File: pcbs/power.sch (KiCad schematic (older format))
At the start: 0 parts

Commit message: LED driver part done.
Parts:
- added J?: Barrel_Jack, Connectors:BARREL_JACK, symbol Barrel_Jack
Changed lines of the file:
@@
 $Descr A4 11693 8268
 encoding utf-8
-Sheet 1 35
+Sheet 35 35
 Title ""
 Date ""
@@
 Comment4 ""
 $EndDescr
-$Sheet
-S 6400 1875 2125 2050
-U 5A0916C5
-F0 "LEDDriver" 60
-F1 "LEDDriver.sch" 60
-$EndSheet
-$Sheet
-S 2380 1810 2170 2300
-U 5A15F128
-F0 "Power" 60
-F1 "power.sch" 60
-$EndSheet
+$Comp
+L Barrel_Jack J?
+U 1 1 5A15F131
+P 1750 1350
+F 0 "J?" H 1750 1560 50  0000 C CNN
+F 1 "Barrel_Jack" H 1750 1175 50  0000 C CNN
+F 2 "Connectors:BARREL_JACK" H 1800 1310 50  0001 C CNN
+F 3 "" H 1800 1310 50  0001 C CNN
+	1    1750 1350
+	1    0    0    -1
+$EndComp
 $EndSCHEMATC

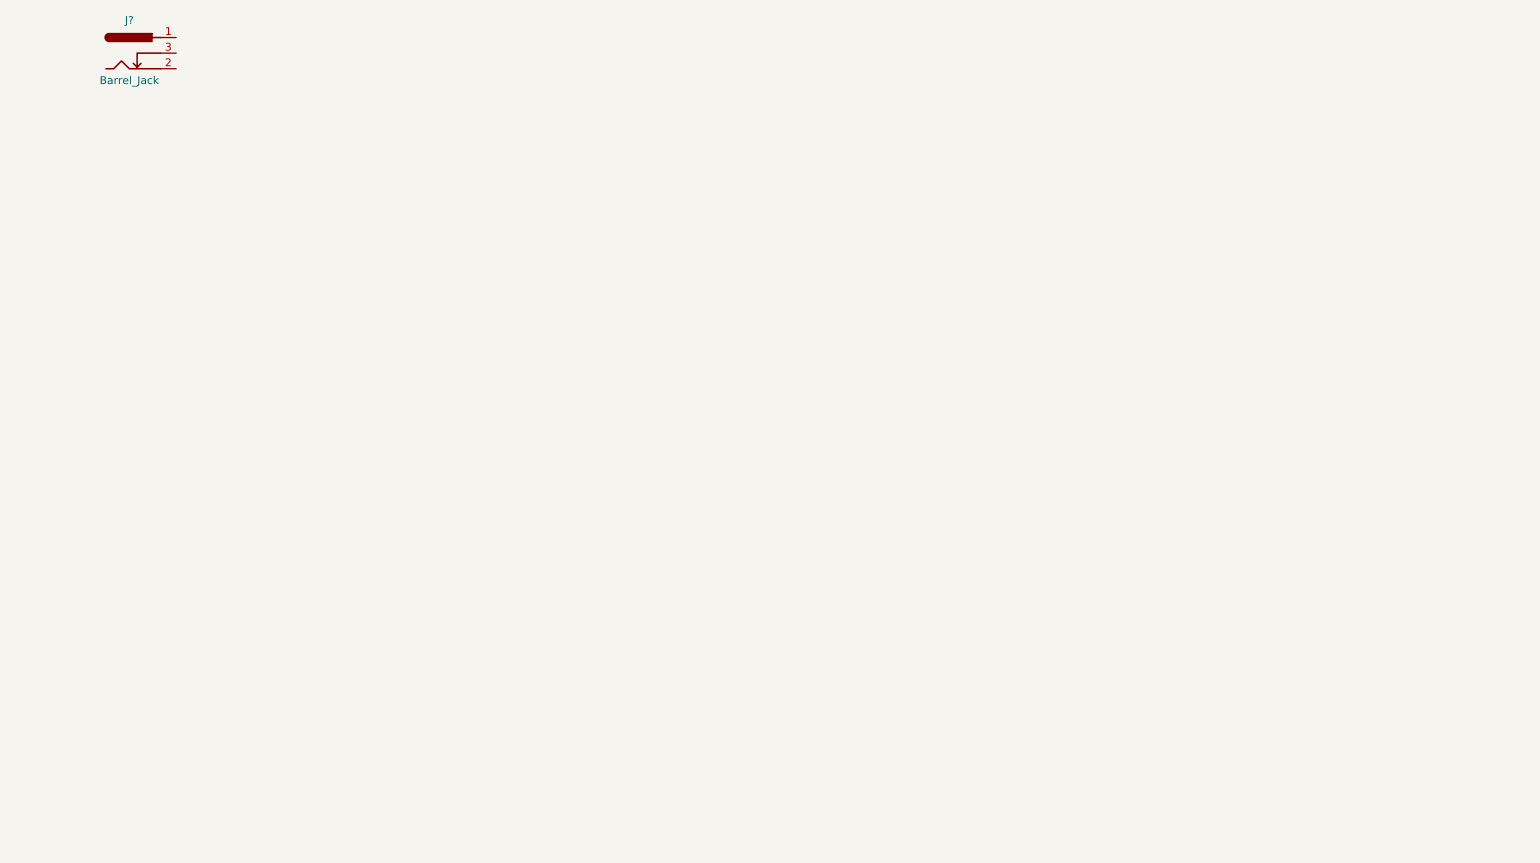
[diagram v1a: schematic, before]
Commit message: Only UI is left for schematics.
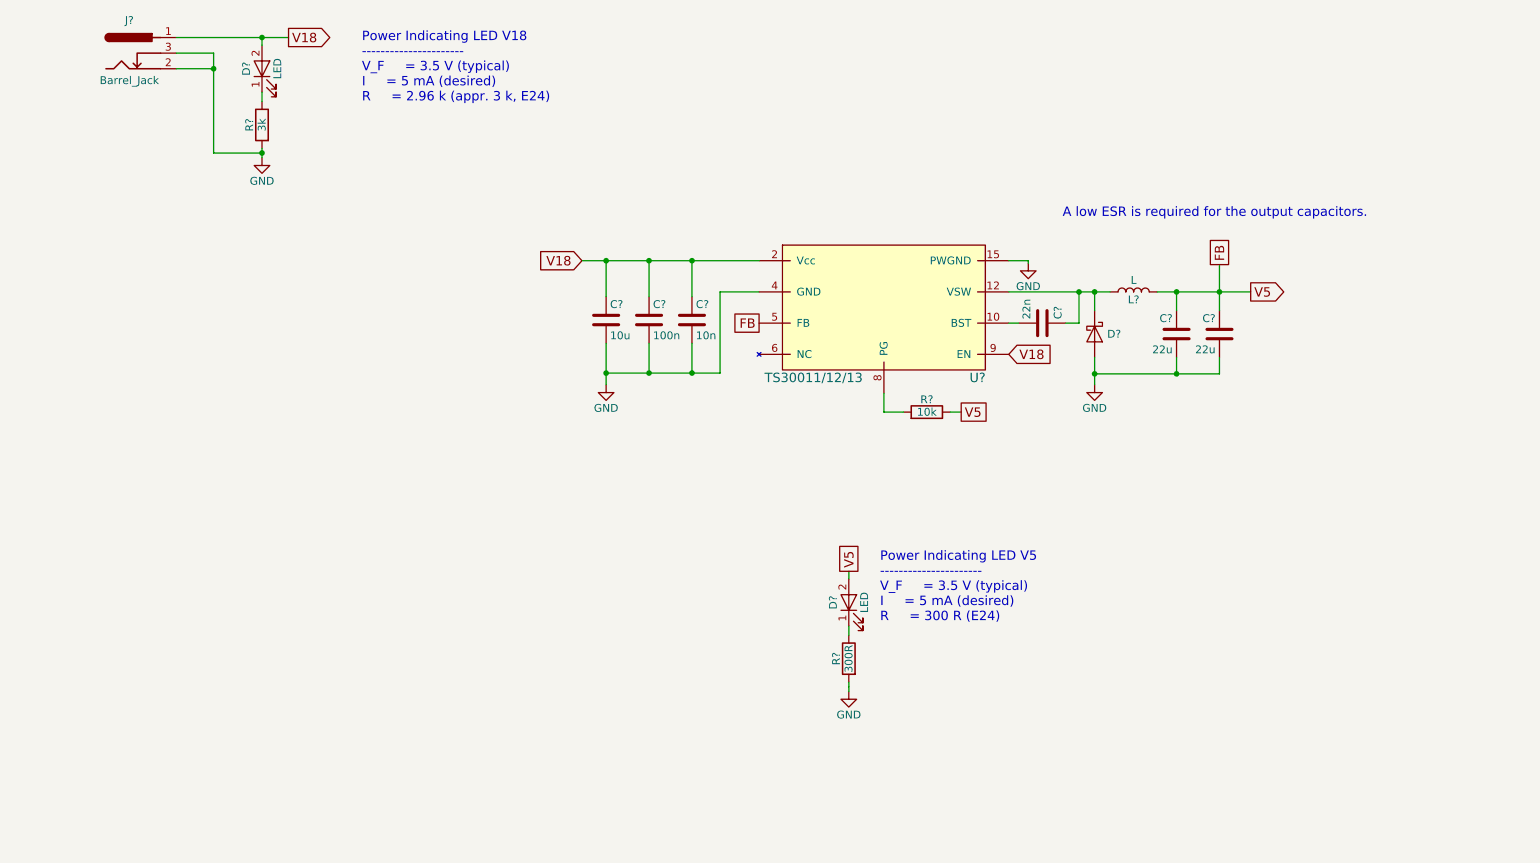
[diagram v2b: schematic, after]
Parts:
- added C? (x2): 22u, Resistors_SMD:R_0805, symbol C
- added C?: 22n, Resistors_SMD:R_0805, symbol C
- added C?: 10n, Resistors_SMD:R_0603, symbol C
- added C?: 100n, Resistors_SMD:R_0603, symbol C
- added C?: 10u, Resistors_SMD:R_0603, symbol C
- added D? (x2): LED, LEDs:LED_0603, symbol LED
- added D?: D_Schottky, Diodes_SMD:D_SOD-123, symbol D_Schottky
- added L?: L, MyInductors:WE-PD2-SMD-Power-Inductor, symbol L
- added R?: 3k, Resistors_SMD:R_0603, symbol R
- added R?: 10k, Resistors_SMD:R_0603, symbol R
- added R?: 300R, Resistors_SMD:R_0603, symbol R
- added U?: TS30011/12/13, QFN:QFN-16-1EP_3x3mm_Pitch0.5mm, symbol TS30011/12/13
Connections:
- net Vcc: now reaches J?.1
- net Vcc: now also C?.1, C?.1, C?.1, D?.2 (A), U?.11 (Vcc), U?.2 (Vcc), U?.3 (Vcc), U?.9 (EN)
- net GND: now reaches J?.2
- net GND: now also J?.3, C?.2, C?.2, C?.2, C?.2, C?.2, D?.2 (A), R?.2, R?.2, U?.14 (PWGND), U?.15 (PWGND), U?.4 (GND)
- new net: D?.1 (K), R?.1 (x2)
- new net: C?.1, D?.1 (K), L?.1, U?.1 (VSW), U?.12 (VSW), U?.13 (VSW), U?.16 (VSW)
- new net: C?.2, U?.10 (BST)
- new net: R?.2, U?.8 (PG)
- new net FB: U?.5 (FB)
- new net V5: C?.1, C?.1, D?.2 (A), L?.2, R?.1
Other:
- note added: "A low ESR is required for the output capacitors."
- note added: "Power Indicating LED V18\n----------------------\nV_F = 3.5 V (typical)\nI = 5 mA (desired)\nR = 2.96 k (appr. 3 k, E24)"
- note added: "Power Indicating LED V5\n----------------------\nV_F = 3.5 V (typical)\nI = 5 mA (desired)\nR = 300 R (E24)"

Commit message: Only UI is left for schematics.
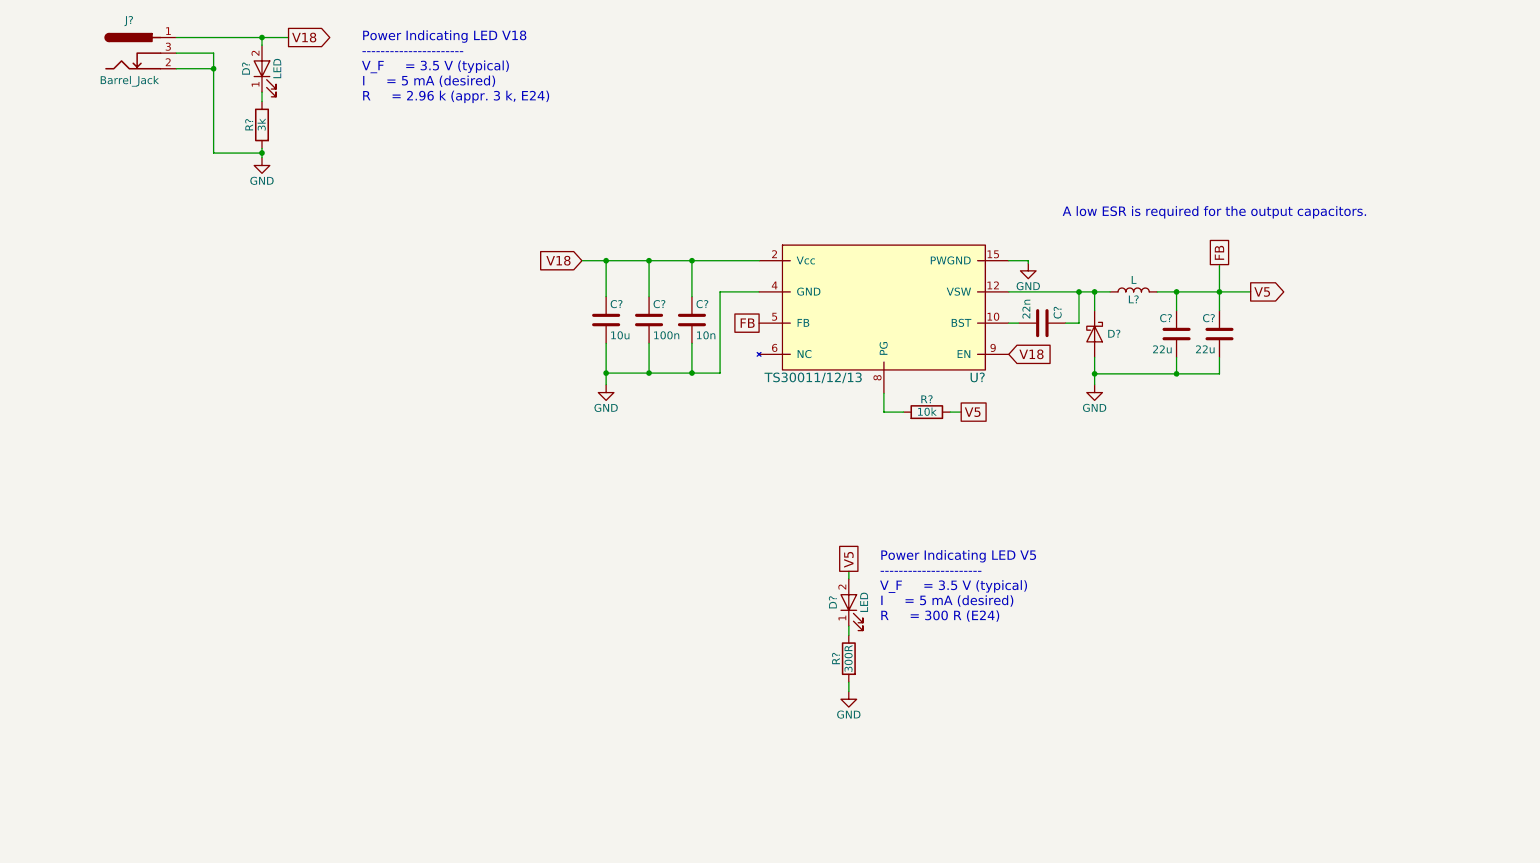
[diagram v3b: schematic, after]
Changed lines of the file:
@@
 $EndComp
 Wire Wire Line
-	2600 1960 2600 1990
-Wire Wire Line
-	2600 1990 2600 2020
+	2600 1960 2600 2020
 Wire Wire Line
 	2600 1660 2600 1600
 Wire Wire Line
-	2050 1250 2600 1250
-Wire Wire Line
-	2600 1250 2770 1250
+	2050 1250 2770 1250
 Wire Wire Line
 	2600 1250 2600 1300
@@
 	2050 1350 2290 1350
 Wire Wire Line
-	2290 1350 2290 1450
-Wire Wire Line
-	2290 1450 2290 1990
+	2290 1350 2290 1990
 Wire Wire Line
 	2290 1990 2600 1990
@@
 $EndComp
 Wire Wire Line
-	7385 2880 7835 2880
-Wire Wire Line
-	7835 2880 7935 2880
-Wire Wire Line
-	7935 2880 8035 2880
+	7385 2880 8035 2880
 Wire Wire Line
 	7450 3080 7385 3080
@@
 $EndComp
 Wire Wire Line
-	7935 3300 7935 3405
-Wire Wire Line
-	7935 3405 7935 3475
+	7935 3300 7935 3475
 Wire Wire Line
 	8460 3300 8460 3405
 Wire Wire Line
-	7935 3405 8460 3405
-Wire Wire Line
-	8460 3405 8735 3405
+	7935 3405 8735 3405
 Wire Wire Line
 	8735 3405 8735 3300
@@
 	8735 2705 8735 2875
 Wire Wire Line
-	8335 2880 8460 2880
-Wire Wire Line
-	8460 2880 8735 2880
-Wire Wire Line
-	8735 2880 8935 2880
+	8335 2880 8935 2880
 $Comp
 L GND #PWR?
@@
 $EndComp
 Wire Wire Line
-	4650 2680 4805 2680
-Wire Wire Line
-	4805 2680 5080 2680
-Wire Wire Line
-	5080 2680 5355 2680
-Wire Wire Line
-	5355 2680 5785 2680
+	4650 2680 5785 2680
 Wire Wire Line
 	4805 2680 4805 2910
@@
 	5355 3400 5355 3210
 Wire Wire Line
-	4805 3400 5080 3400
-Wire Wire Line
-	5080 3400 5355 3400
-Wire Wire Line
-	5355 3400 5535 3400
-Wire Wire Line
-	4805 3210 4805 3400
-Wire Wire Line
-	4805 3400 4805 3475
+	4805 3400 5535 3400
+Wire Wire Line
+	4805 3210 4805 3475
 Connection ~ 4805 3400
 Wire Wire Line
@@
 $EndComp
 Wire Wire Line
-	6360 5380 6360 5410
-Wire Wire Line
-	6360 5410 6360 5440
+	6360 5380 6360 5440
 Wire Wire Line
 	6360 5080 6360 5020

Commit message: Almost done with schematics. SPI OLED is missing.
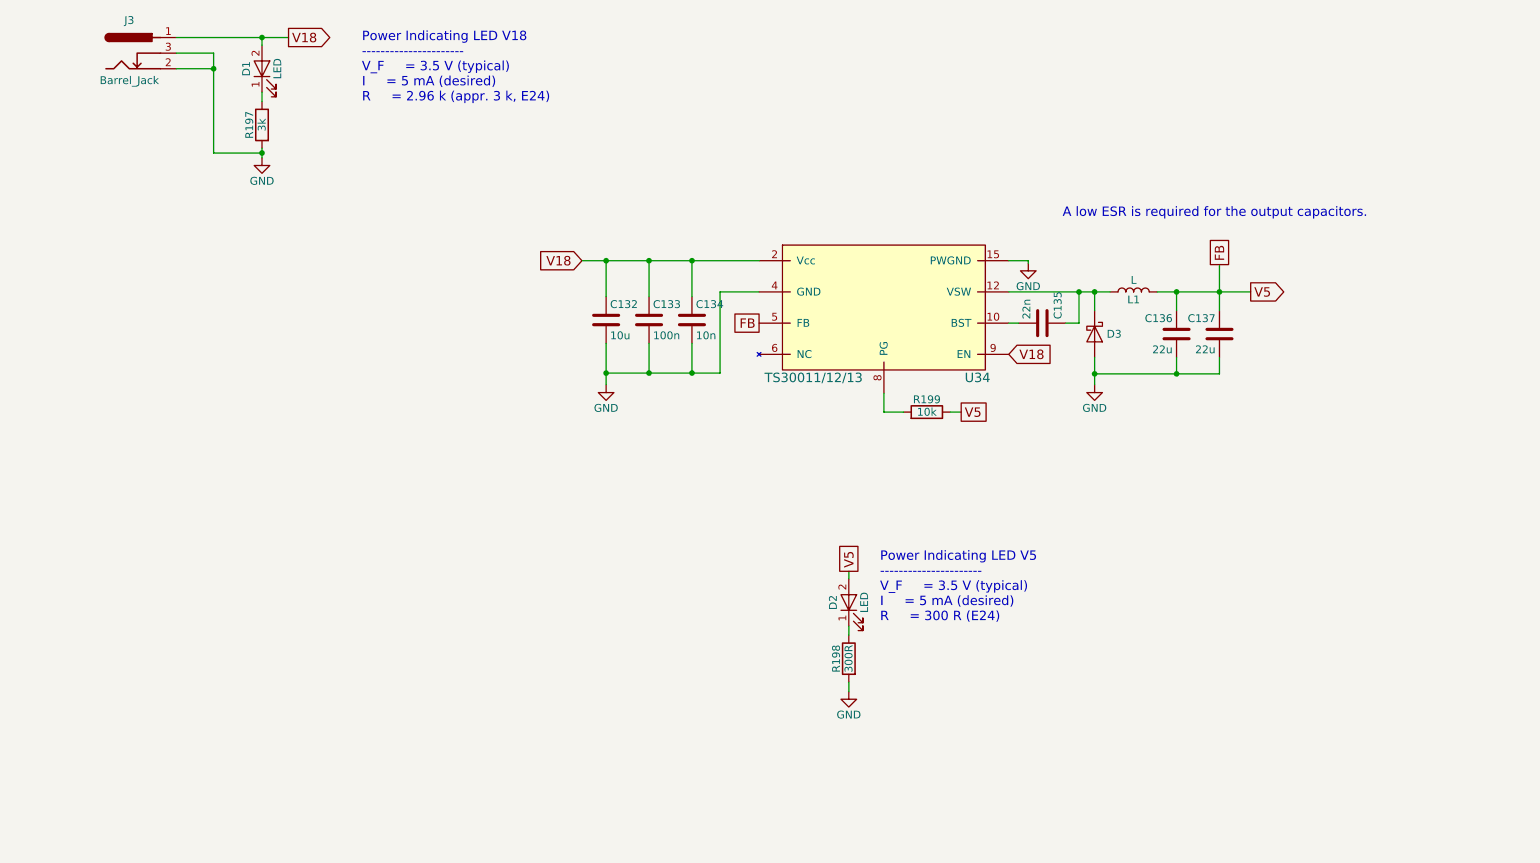
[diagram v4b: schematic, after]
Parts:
- gave numbers to parts that had none: 15
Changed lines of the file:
@@
 LIBS:mydacs
 LIBS:mydcdcs
+LIBS:switches
+LIBS:mytactilesw
 LIBS:led_driver-cache
 EELAYER 25 0
@@
 $EndDescr
 $Comp
-L Barrel_Jack J?
+L Barrel_Jack J3
 U 1 1 5A15F131
 P 1750 1350
-F 0 "J?" H 1750 1560 50  0000 C CNN
+F 0 "J3" H 1750 1560 50  0000 C CNN
 F 1 "Barrel_Jack" H 1750 1175 50  0000 C CNN
 F 2 "Connectors:BARREL_JACK" H 1800 1310 50  0001 C CNN
@@
 $EndComp
 $Comp
-L LED D?
+L LED D1
 U 1 1 5A0AC005
 P 2600 1450
-F 0 "D?" H 2600 1550 50  0000 C CNN
+F 0 "D1" H 2600 1550 50  0000 C CNN
 F 1 "LED" H 2600 1350 50  0000 C CNN
 F 2 "LEDs:LED_0603" H 2600 1450 50  0001 C CNN
@@
 Power Indicating LED V18\n----------------------\nV_F 	= 3.5 V (typical)\nI 	= 5 mA (desired)\nR 	= 2.96 k (appr. 3 k, E24)
 $Comp
-L R R?
+L R R197
 U 1 1 5A0AD655
 P 2600 1810
-F 0 "R?" V 2680 1810 50  0000 C CNN
+F 0 "R197" V 2680 1810 50  0000 C CNN
 F 1 "3k" V 2600 1810 50  0000 C CNN
 F 2 "Resistors_SMD:R_0603" V 2530 1810 50  0001 C CNN
@@
 $EndComp
 $Comp
-L GND #PWR?
+L GND #PWR324
 U 1 1 5A0AD8CE
 P 2600 2020
-F 0 "#PWR?" H 2600 1770 50  0001 C CNN
+F 0 "#PWR324" H 2600 1770 50  0001 C CNN
 F 1 "GND" H 2600 1870 50  0000 C CNN
 F 2 "" H 2600 2020 50  0001 C CNN
@@
 Connection ~ 2600 1250
 $Comp
-L L L?
+L L L1
 U 1 1 5A0AFB54
 P 8185 2880
-F 0 "L?" V 8135 2880 50  0000 C CNN
+F 0 "L1" V 8135 2880 50  0000 C CNN
 F 1 "L" V 8260 2880 50  0000 C CNN
 F 2 "MyInductors:WE-PD2-SMD-Power-Inductor" H 8185 2880 50  0001 C CNN
@@
 $EndComp
 $Comp
-L C C?
+L C C136
 U 1 1 5A0B087F
 P 8460 3150
-F 0 "C?" H 8485 3250 50  0000 L CNN
+F 0 "C136" H 8485 3250 50  0000 L CNN
 F 1 "22u" H 8485 3050 50  0000 L CNN
 F 2 "Resistors_SMD:R_0805" H 8498 3000 50  0001 C CNN
@@
 $EndComp
 $Comp
-L C C?
+L C C137
 U 1 1 5A0B15B3
 P 8735 3150
-F 0 "C?" H 8760 3250 50  0000 L CNN
+F 0 "C137" H 8760 3250 50  0000 L CNN
 F 1 "22u" H 8760 3050 50  0000 L CNN
 F 2 "Resistors_SMD:R_0805" H 8773 3000 50  0001 C CNN
@@
 $EndComp
 $Comp
-L C C?
+L C C135
 U 1 1 5A0B64DA
 P 7600 3080
-F 0 "C?" H 7625 3180 50  0000 L CNN
+F 0 "C135" H 7625 3180 50  0000 L CNN
 F 1 "22n" H 7625 2980 50  0000 L CNN
 F 2 "Resistors_SMD:R_0805" H 7638 2930 50  0001 C CNN
@@
 $EndComp
 $Comp
-L TS30011/12/13 U?
+L TS30011/12/13 U34
 U 1 1 5A0B688D
 P 6535 2980
-F 0 "U?" H 7185 2530 60  0000 C CNN
+F 0 "U34" H 7185 2530 60  0000 C CNN
 F 1 "TS30011/12/13" H 6135 2530 60  0000 C CNN
 F 2 "QFN:QFN-16-1EP_3x3mm_Pitch0.5mm" H 6685 2980 60  0001 C CNN
@@
 Connection ~ 8460 2880
 $Comp
-L D_Schottky D?
+L D_Schottky D3
 U 1 1 5A0B72C0
 P 7935 3150
-F 0 "D?" V 7935 3275 50  0000 C CNN
+F 0 "D3" V 7935 3275 50  0000 C CNN
 F 1 "D_Schottky" V 7935 3425 50  0001 C CNN
 F 2 "Diodes_SMD:D_SOD-123" H 7935 3150 50  0001 C CNN
@@
 V18
 $Comp
-L GND #PWR?
+L GND #PWR328
 U 1 1 5A0B8173
 P 7935 3475
-F 0 "#PWR?" H 7935 3225 50  0001 C CNN
+F 0 "#PWR328" H 7935 3225 50  0001 C CNN
 F 1 "GND" H 7935 3325 50  0000 C CNN
 F 2 "" H 7935 3475 50  0001 C CNN
@@
 FB
 $Comp
-L GND #PWR?
+L GND #PWR327
 U 1 1 5A0B8CE5
 P 7510 2695
-F 0 "#PWR?" H 7510 2445 50  0001 C CNN
+F 0 "#PWR327" H 7510 2445 50  0001 C CNN
 F 1 "GND" H 7510 2545 50  0000 C CNN
 F 2 "" H 7510 2695 50  0001 C CNN
@@
 	8335 2880 8935 2880
 $Comp
-L GND #PWR?
+L GND #PWR325
 U 1 1 5A0BC4D5
 P 4805 3475
-F 0 "#PWR?" H 4805 3225 50  0001 C CNN
+F 0 "#PWR325" H 4805 3225 50  0001 C CNN
 F 1 "GND" H 4805 3325 50  0000 C CNN
 F 2 "" H 4805 3475 50  0001 C CNN
@@
 $EndComp
 $Comp
-L C C?
+L C C134
 U 1 1 5A0BC504
 P 5355 3060
-F 0 "C?" H 5380 3160 50  0000 L CNN
+F 0 "C134" H 5380 3160 50  0000 L CNN
 F 1 "10n" H 5380 2960 50  0000 L CNN
 F 2 "Resistors_SMD:R_0603" H 5393 2910 50  0001 C CNN
@@
 $EndComp
 $Comp
-L C C?
+L C C133
 U 1 1 5A0BC63E
 P 5080 3060
-F 0 "C?" H 5105 3160 50  0000 L CNN
+F 0 "C133" H 5105 3160 50  0000 L CNN
 F 1 "100n" H 5105 2960 50  0000 L CNN
 F 2 "Resistors_SMD:R_0603" H 5118 2910 50  0001 C CNN
@@
 $EndComp
 $Comp
-L C C?
+L C C132
 U 1 1 5A0BC687
 P 4805 3060
-F 0 "C?" H 4830 3160 50  0000 L CNN
+F 0 "C132" H 4830 3160 50  0000 L CNN
 F 1 "10u" H 4830 2960 50  0000 L CNN
 F 2 "Resistors_SMD:R_0603" H 4843 2910 50  0001 C CNN
@@
 A low ESR is required for the output capacitors.
 $Comp
-L R R?
+L R R199
 U 1 1 5A0C01F9
 P 6860 3650
-F 0 "R?" V 6940 3650 50  0000 C CNN
+F 0 "R199" V 6940 3650 50  0000 C CNN
 F 1 "10k" V 6860 3650 50  0000 C CNN
 F 2 "Resistors_SMD:R_0603" V 6790 3650 50  0001 C CNN
@@
 	6585 3650 6585 3530
 $Comp
-L LED D?
+L LED D2
 U 1 1 5A0C1EDB
 P 6360 4870
-F 0 "D?" H 6360 4970 50  0000 C CNN
+F 0 "D2" H 6360 4970 50  0000 C CNN
 F 1 "LED" H 6360 4770 50  0000 C CNN
 F 2 "LEDs:LED_0603" H 6360 4870 50  0001 C CNN
@@
 $EndComp
 $Comp
-L R R?
+L R R198
 U 1 1 5A0C1EE2
 P 6360 5230
-F 0 "R?" V 6440 5230 50  0000 C CNN
+F 0 "R198" V 6440 5230 50  0000 C CNN
 F 1 "300R" V 6360 5230 50  0000 C CNN
 F 2 "Resistors_SMD:R_0603" V 6290 5230 50  0001 C CNN
@@
 $EndComp
 $Comp
-L GND #PWR?
+L GND #PWR326
 U 1 1 5A0C1EE8
 P 6360 5440
-F 0 "#PWR?" H 6360 5190 50  0001 C CNN
+F 0 "#PWR326" H 6360 5190 50  0001 C CNN
 F 1 "GND" H 6360 5290 50  0000 C CNN
 F 2 "" H 6360 5440 50  0001 C CNN
